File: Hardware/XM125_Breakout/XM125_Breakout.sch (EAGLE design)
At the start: 55 parts, among them J2 QWIIC_RIGHT_ANGLE, J3 QWIIC_RIGHT_ANGLE, U1 XM125, U2 RT9080-33GJ5, U3 RT9080-18GJ5, U4 CH340C, U5 ESD Diode

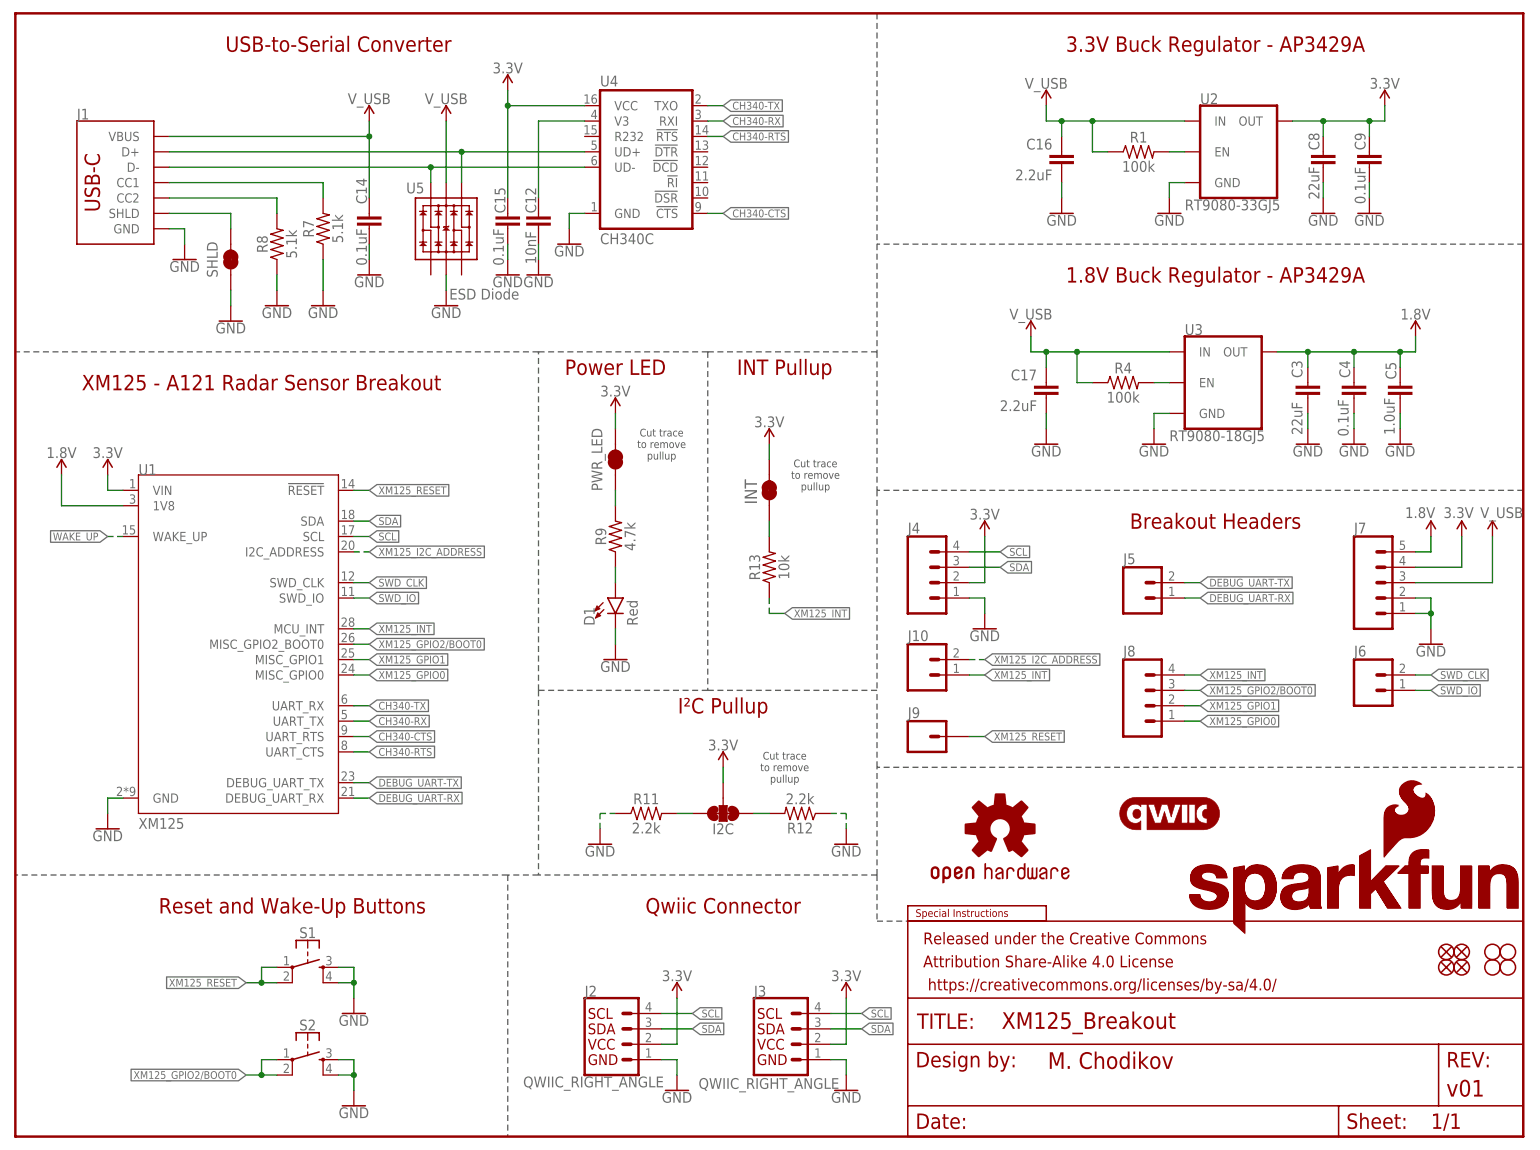
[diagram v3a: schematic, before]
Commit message: Updated files for design review
Nearing completion and ready for design review - completed layout, added measures, added labels, name, logos
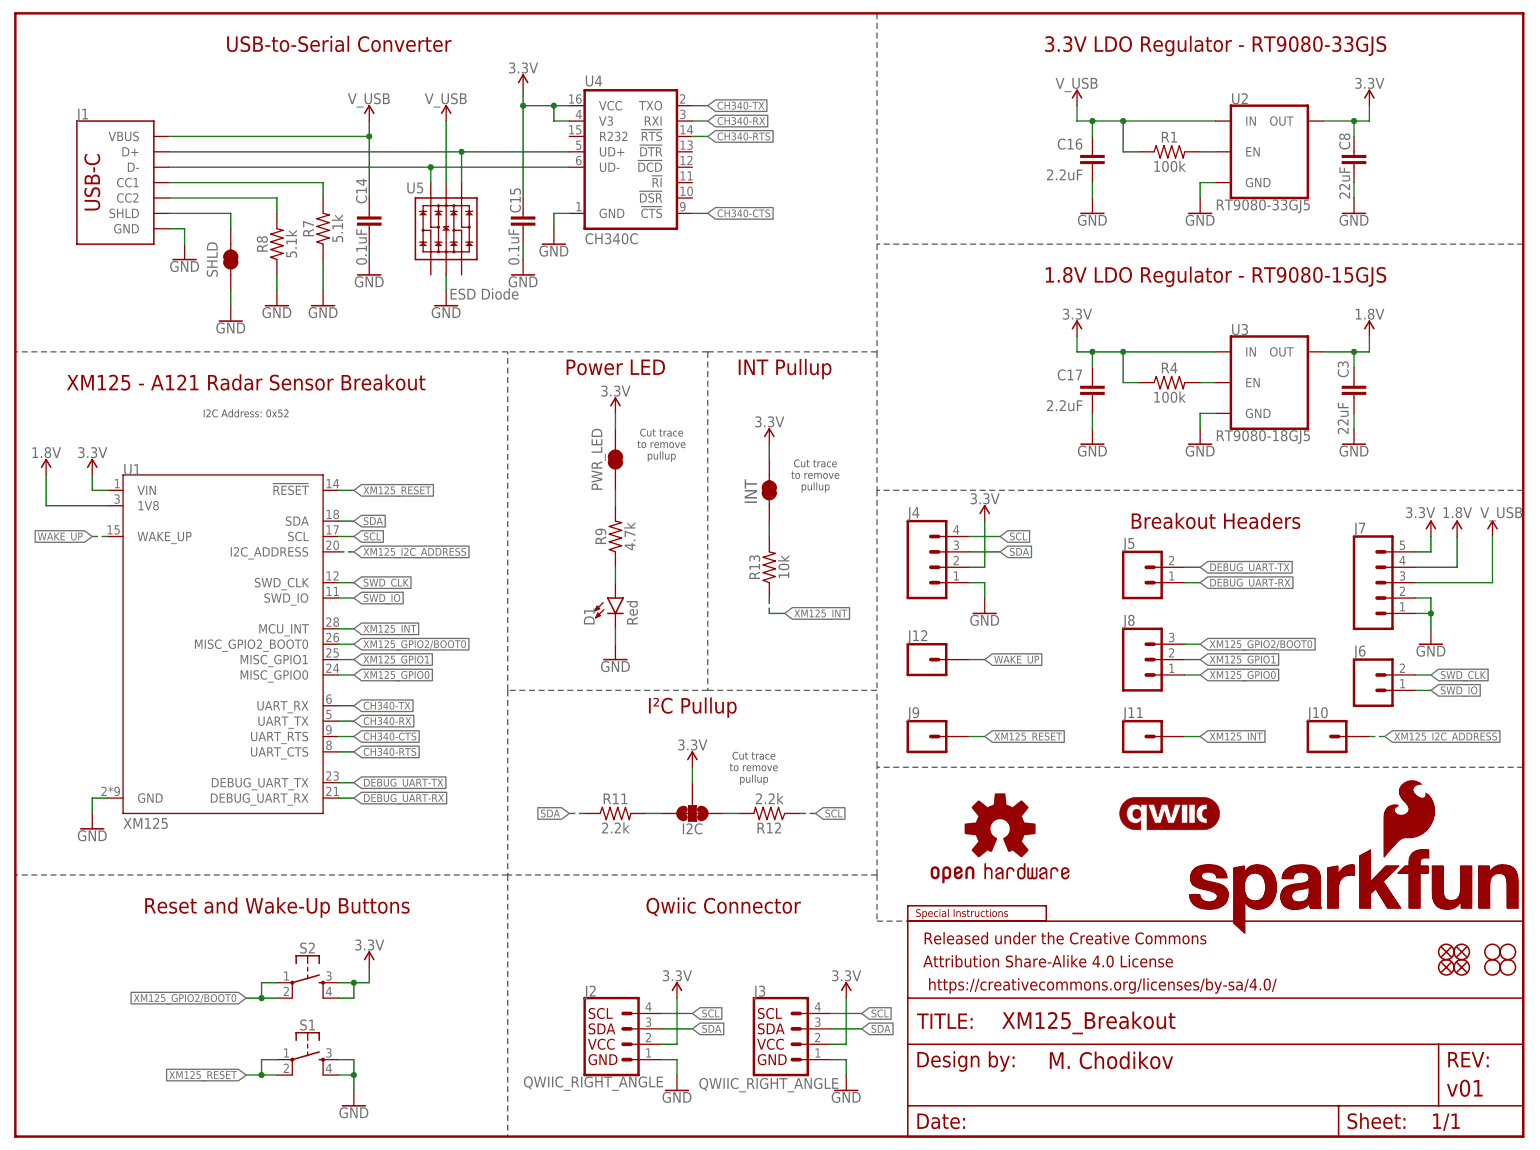
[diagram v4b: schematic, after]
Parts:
- removed C12: 10nF, SparkFun-Capacitors:10NF-0603-50V-10%
- removed C4, C9: 0.1uF, SparkFun-Capacitors:0.1UF-0603-25V-5%
- removed C5: 1.0uF, SparkFun-Capacitors:1.0UF-0603-16V-10%-X7R
- added J11, J12: (no value), SparkFun-Connectors:CONN_01PTH_NO_SILK_STAND
- J10: device SparkFun-Connectors:CONN_021X02_NO_SILK -> SparkFun-Connectors:CONN_01PTH_NO_SILK_STAND
- J8: device SparkFun-Connectors:CONN_041X04_NO_SILK -> SparkFun-Connectors:CONN_031X03_NO_SILK
- LOGO2: value QWIIC_LOGO_3MM -> QWIIC_LOGO_4MM; device SparkFun-Aesthetics:QWIIC_LOGO_3MM -> SparkFun-Aesthetics:QWIIC_LOGO_4MM
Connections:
- removed net N$12: C12.1, U4.V3
- net 1.8V: now also J7.4; no longer C4.1, C5.1, J7.5
- net 3.3V: now also C17.1, J7.5, R4.1, S2.3, S2.4, U3.IN, U4.V3; no longer C9.1, J7.4
- net GND: no longer C12.2, C4.2, C5.2, C9.2, R11.1, R12.1, S2.3, S2.4
- net SCL: now also R12.1
- net SDA: now also R11.1
- net V_USB: no longer C17.1, R4.1, U3.IN
- net WAKE_UP: now also J12.1
- net XM125_I2C_ADDRESS: now also J10.1; no longer J10.2
- net XM125_INT: now also J11.1; no longer J10.1, J8.4
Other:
- note added: "1.8V LDO Regulator - RT9080-15GJS"
- note added: "3.3V LDO Regulator - RT9080-33GJS"
- note added: "I2C Address: 0x52"
- note removed: "1.8V Buck Regulator - AP3429A"
- note removed: "3.3V Buck Regulator - AP3429A"
- moved on the sheet: C15, C16, C17, C3, C8, I2C, J4, J5, R1, R11, R12, R4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

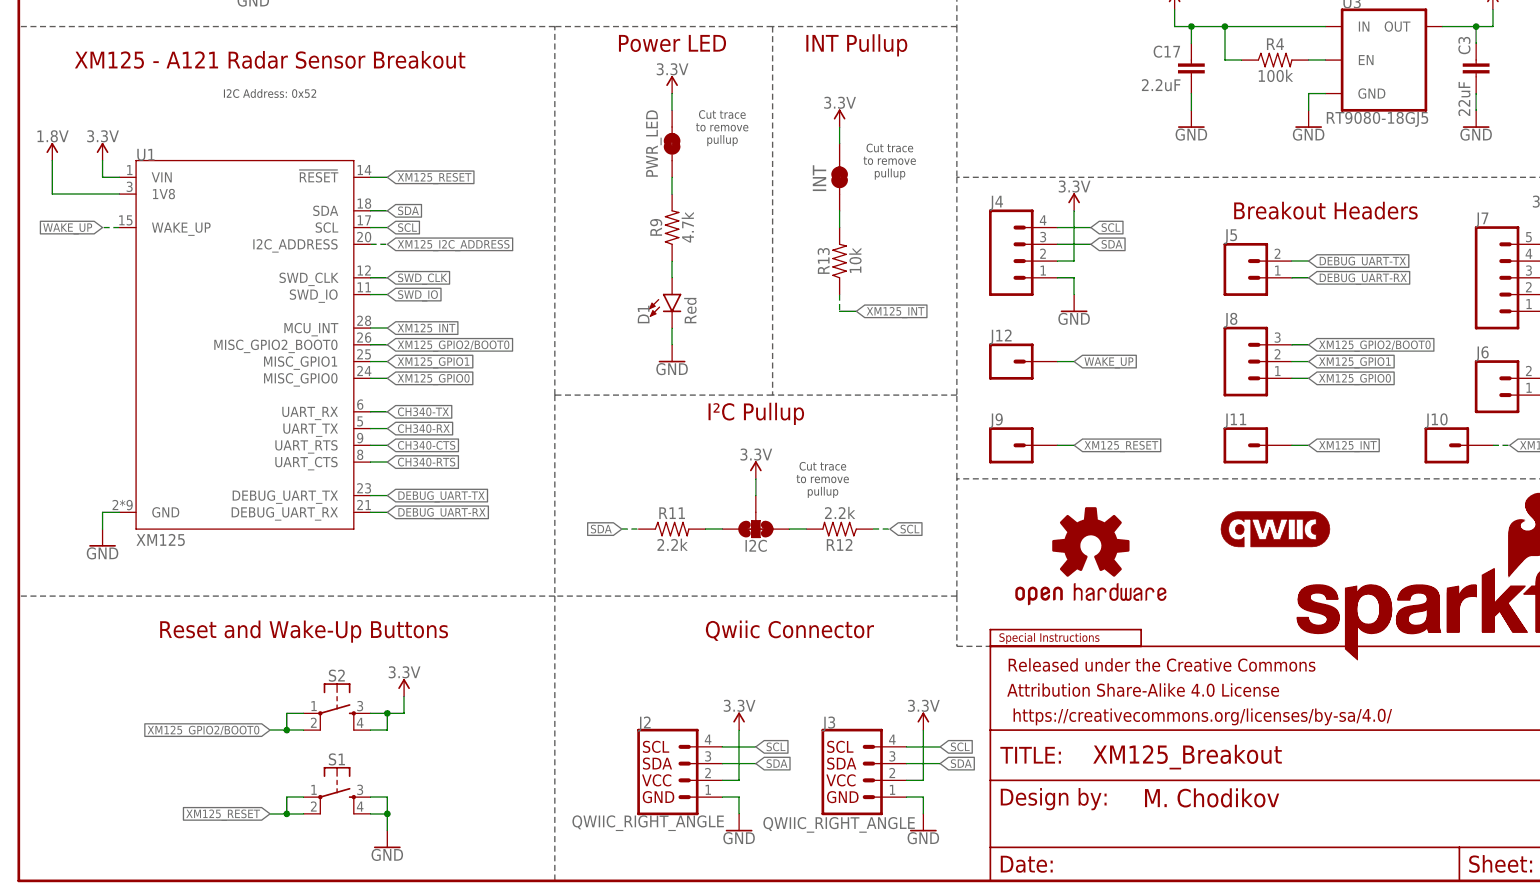
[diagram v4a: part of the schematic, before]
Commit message: Changes from design review
Final changes made - ready for re-review one last time before ordering protos
For full list of changes, see Protos Review document
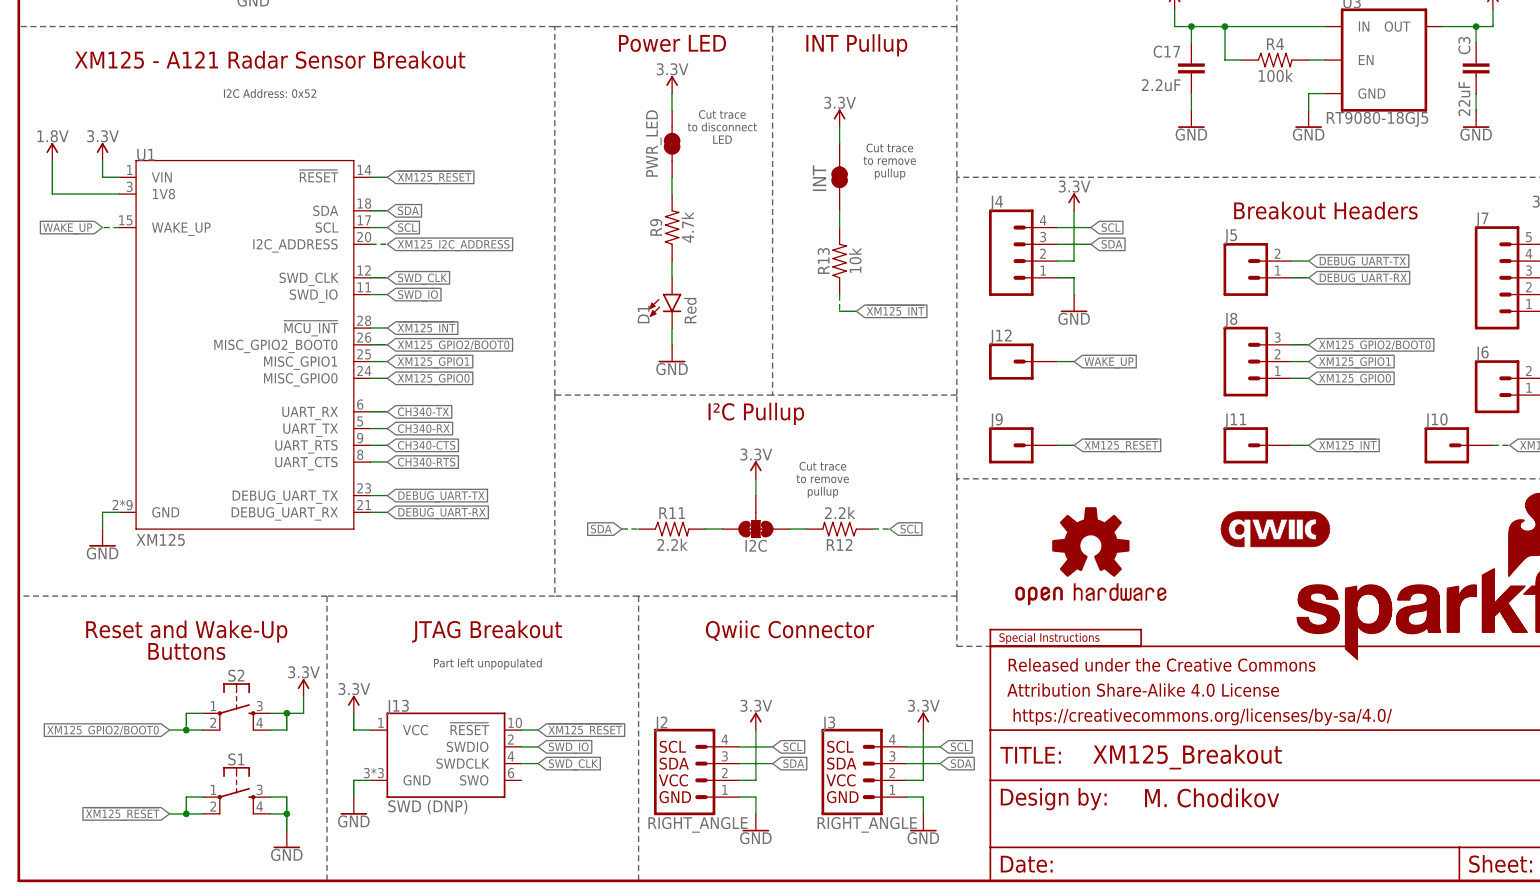
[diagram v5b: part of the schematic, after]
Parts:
- added J13: SWD (DNP), SparkFun-Connectors:CORTEX_JTAG_DEBUG_MINIMUM_SMD_UNSHROUDED_DNP_NO_PASTE
- J2, J3: value QWIIC_RIGHT_ANGLE -> RIGHT_ANGLE
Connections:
- removed net XM125_INT: J11.1, R13.1, U1.MCU_INT
- removed net XM125_RESET: J9.1, S1.1, S1.2, U1.!RESET
- new net !XM125_INT: J11.1, R13.1, U1.!MCU_INT
- new net !XM125_RESET: J13.!RESET, J9.1, S1.1, S1.2, U1.!RESET
- net 3.3V: now also J13.VCC
- net GND: now also J13.GND
- net SWD_CLK: now also J13.SWDCLK
- net SWD_IO: now also J13.SWDIO
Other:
- note added: "Buttons"
- note added: "Cut trace to disconnect LED"
- note added: "JTAG Breakout"
- note added: "Part left unpopulated"
- note added: "Reset and Wake-Up"
- note removed: "Reset and Wake-Up Buttons"
- moved on the sheet: J2, S1, S2

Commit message: Production files added
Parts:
- LOGO6: value SFE_LOGO_NAME.1_INCH -> SFE_LOGO_NAME_FLAME.1_INCH; device SparkFun-Aesthetics:SFE_LOGO_NAME.1_INCH -> SparkFun-Aesthetics:SFE_LOGO_NAME_FLAME.1_INCH
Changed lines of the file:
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@@
 <part name="LOGO4" library="SparkFun-Aesthetics" deviceset="OSHW-LOGO" device="S"/>
 <part name="LOGO5" library="SparkFun-Aesthetics" deviceset="SFE_LOGO_FLAME" device=".1_INCH"/>
-<part name="LOGO6" library="SparkFun-Aesthetics" deviceset="SFE_LOGO_NAME" device=".1_INCH"/>
+<part name="LOGO6" library="SparkFun-Aesthetics" deviceset="SFE_LOGO_NAME_FLAME" device=".1_INCH"/>
 <part name="GND1" library="SparkFun-PowerSymbols" deviceset="GND" device=""/>
 <part name="SUPPLY1" library="SparkFun-PowerSymbols" deviceset="1.8V" device=""/>
